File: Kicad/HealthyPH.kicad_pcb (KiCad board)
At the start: 2 copper layers, 68.6 x 53.4 mm, 48 parts, among them CON1 LB_BarrelJack, P1 CONN_8, P2 WallWartExtension, Q1 TIP122, Q2 TIP122, U1 MCP6241, U2 MCP3901, U3 MC78L05, X1 CRYSTAL

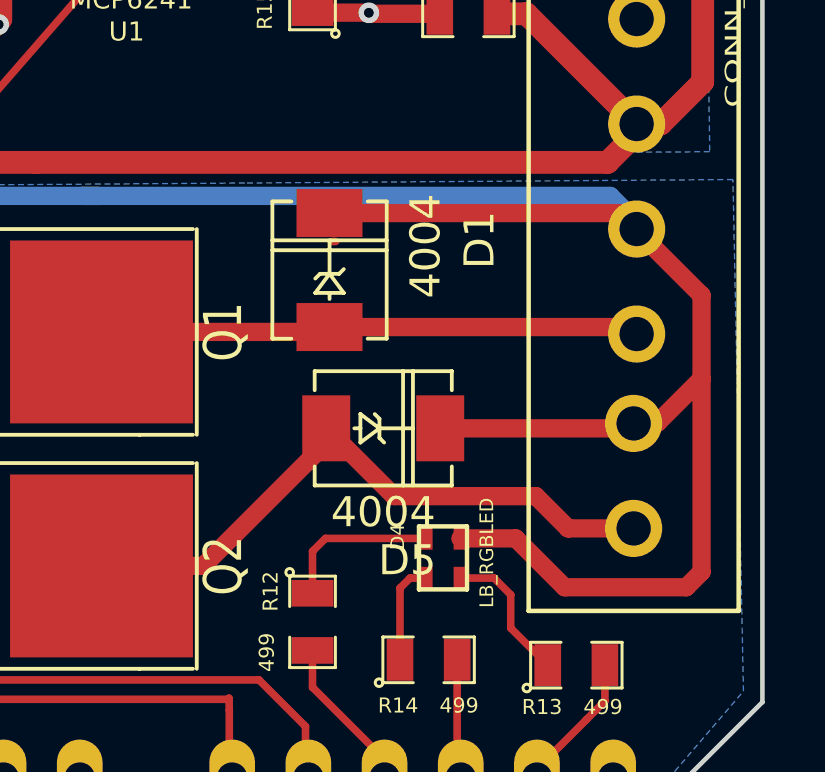
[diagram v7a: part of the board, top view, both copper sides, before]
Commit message: first pass changing ADC
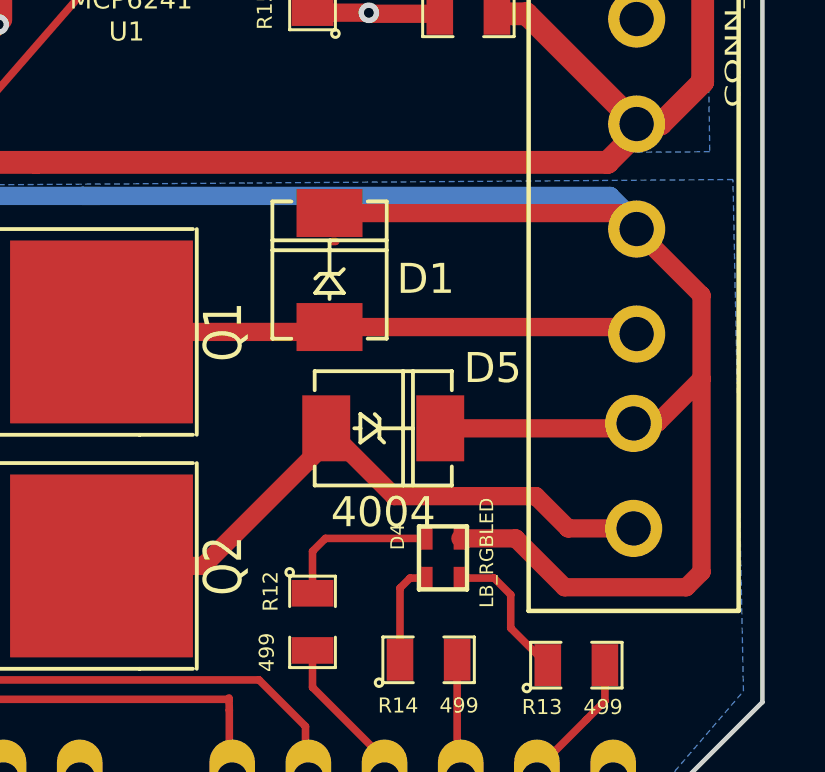
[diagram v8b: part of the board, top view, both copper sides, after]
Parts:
- D1: value 4004 -> (none)
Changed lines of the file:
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@@
   )
   (setup
-    (last_trace_width 0.6096)
+    (last_trace_width 0.254)
     (user_trace_width 0.254)
     (user_trace_width 0.6096)
@@
     (tags "DO-214AC SMA")
     (attr smd)
-    (fp_text reference D1 (at 1 5 90) (layer F.SilkS)
+    (fp_text reference D1 (at -0.29718 3.20548 180) (layer F.SilkS)
       (effects (font (size 1.00076 1.00076) (thickness 0.11938)))
     )
-    (fp_text value 4004 (at 0.8 3.2 90) (layer F.SilkS)
+    (fp_text value "" (at 0.8 3.2 90) (layer F.SilkS)
       (effects (font (size 1.00076 1.00076) (thickness 0.11938)))
     )
@@
     (tags "DO-214AC SMA")
     (attr smd)
-    (fp_text reference D5 (at 0.8 4.4) (layer F.SilkS)
+    (fp_text reference D5 (at 3.64998 -2.0066) (layer F.SilkS)
       (effects (font (size 1.00076 1.00076) (thickness 0.11938)))
     )
@@
   (segment (start 195.36664 95.1484) (end 184.2262 95.1484) (width 0.762) (layer F.Cu) (net 12))
   (segment (start 184.2262 95.1484) (end 184.0484 95.1484) (width 0.6096) (layer F.Cu) (net 12))
-  (segment (start 202.47864 84.91728) (end 199.62622 84.91728) (width 0.254) (layer F.Cu) (net 13) (status C00000))
-  (segment (start 199.62622 84.91728) (end 199.5805 84.963) (width 0.254) (layer F.Cu) (net 13) (status C00000))
+  (segment (start 202.47864 84.91728) (end 199.62622 84.91728) (width 0.254) (layer F.Cu) (net 13))
+  (segment (start 199.62622 84.91728) (end 199.5805 84.963) (width 0.254) (layer F.Cu) (net 13))
   (segment (start 197.6755 87.503) (end 197.6755 87.05342) (width 0.254) (layer F.Cu) (net 13))
   (segment (start 199.5805 86.30412) (end 199.5805 84.963) (width 0.254) (layer F.Cu) (net 13))
@@
   (segment (start 203.1196 86.86966) (end 215.38798 86.86966) (width 0.254) (layer F.Cu) (net 22))
   (segment (start 202.48626 87.503) (end 203.1196 86.86966) (width 0.254) (layer F.Cu) (net 22))
-  (segment (start 187.7671 82.20932) (end 188.81312 82.20932) (width 0.254) (layer F.Cu) (net 23) (status 400000))
+  (segment (start 187.7671 82.20932) (end 188.81312 82.20932) (width 0.254) (layer F.Cu) (net 23))
   (segment (start 188.82106 82.21726) (end 188.82106 82.21218) (width 0.254) (layer B.Cu) (net 23))
   (via (at 188.82106 82.21726) (size 0.6858) (layers F.Cu B.Cu) (net 23))
